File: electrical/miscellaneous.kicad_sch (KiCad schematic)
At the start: 1 part

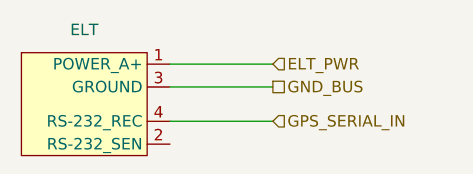
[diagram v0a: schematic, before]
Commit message: Changed grounds and canbuses to be in/out when applicable.
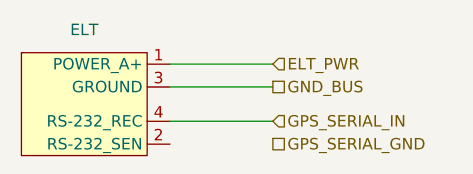
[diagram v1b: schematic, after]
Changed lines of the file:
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@@
     (stroke (width 0) (type default))
+  )
+  (hierarchical_label "GPS_SERIAL_GND" (shape passive) (at 147.32 92.71 0) (fields_autoplaced)
+    (effects (font (size 1.27 1.27)) (justify left))
   )
   (hierarchical_label "GND_BUS" (shape passive) (at 147.32 86.36 0) (fields_autoplaced)
